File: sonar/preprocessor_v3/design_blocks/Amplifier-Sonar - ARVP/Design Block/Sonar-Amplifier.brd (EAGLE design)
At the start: 20 x 20 mm, 11 parts, among them U1 AD8336ACPZ-R7

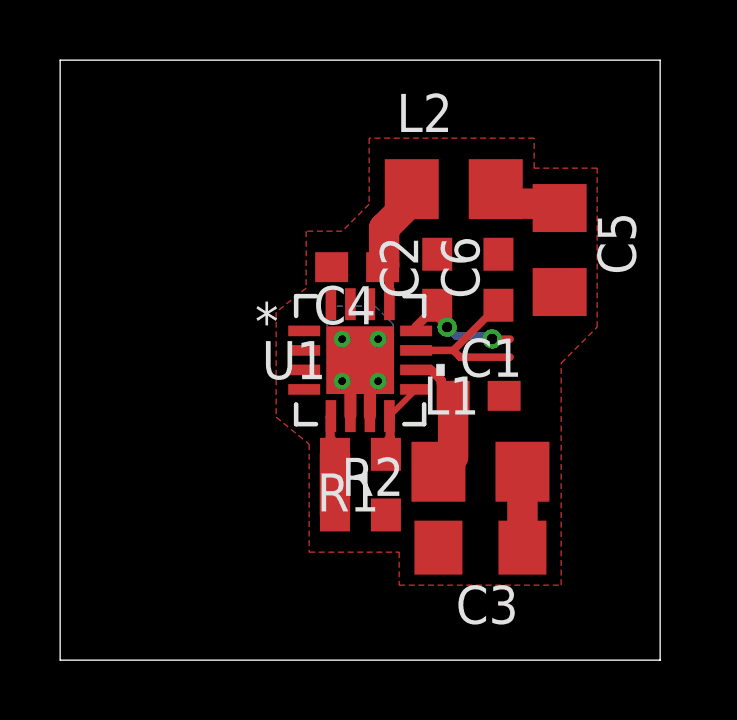
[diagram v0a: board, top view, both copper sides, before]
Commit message: Added a little bit more clearance
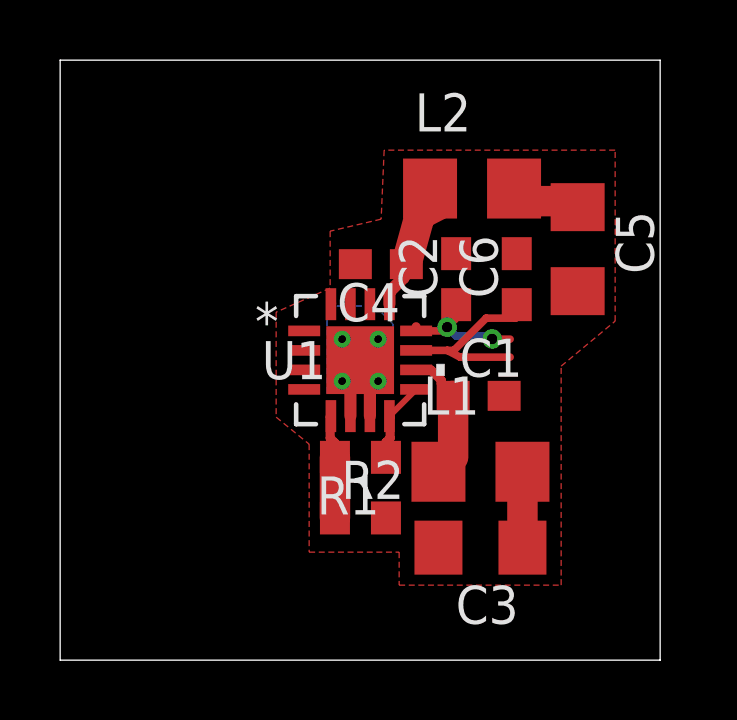
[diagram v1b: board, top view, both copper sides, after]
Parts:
- moved C4 0.80 mm to (10.7, 13.2)
- moved C2 0.63 mm to (13.2, 12.7)
- moved C6 0.61 mm to (15.2, 12.7)
- moved L2 0.61 mm to (13.7, 15.7)
- moved C5 0.60 mm to (17.2, 13.7)
- moved R1 0.10 mm to (10.0, 6.76)
- moved R2 0.10 mm to (10.0, 4.74)
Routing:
- net GAIN_POS: track 5.36 -> 6.36 mm
